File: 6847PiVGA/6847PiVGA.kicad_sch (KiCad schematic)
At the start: 51 parts, among them J1 DB15_Female_HighDensity, J2 Conn_01x06_Male, U1 MC6847, U2 AD724JRZ, U3 Pico, U4 AD813, U5 TXS0108EPW, U6 TXS0108EPW, U7 TXS0108EPW, Y1 4.433620MHz

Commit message: route out board
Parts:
- removed C11: 10uF, Capacitor_SMD:C_0805_2012Metric, symbol Device:C
- removed D1: 1N5817, Diode_SMD:D_0805_2012Metric_Pad1.15x1.40mm_HandSolder, symbol Diode:1N5817
- removed U3: Pico, Package_DIP:DIP-40_W15.24mm, symbol MCU_RaspberryPi_and_Boards:Pico
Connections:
- net +3.3V: no longer U5.10 (OE), U6.10 (OE), U7.10 (OE)
- net DD0: now also U5.14 (B6); no longer U5.20 (B1)
- net DD1: now also U5.15 (B5); no longer U5.18 (B2)
- net DD2: now also U5.16 (B4); no longer U5.17 (B3)
- net DD3: now also U5.17 (B3); no longer U5.16 (B4)
- net DD4: now also U5.18 (B2); no longer U5.15 (B5)
- net DD5: now also U5.20 (B1); no longer U5.14 (B6)
- net DL0: now also U5.7 (A6); no longer U5.1 (A1)
- net DL1: now also U5.6 (A5); no longer U5.3 (A2)
- net DL2: now also U5.5 (A4); no longer U5.4 (A3)
- net DL3: now also U5.4 (A3); no longer U5.5 (A4)
- net DL4: now also U5.3 (A2); no longer U5.6 (A5)
- net DL5: now also U5.1 (A1); no longer U5.7 (A6)
- net GND: no longer R23.2
- net G2: now reaches R6.2
- net G1: now reaches R5.2
- net B0: now reaches R7.2
- net R2: now reaches R3.2
- net B2: now reaches R9.2
- net B1: now reaches R8.2
- net G0: now reaches R4.2
- net R0: now reaches R1.2
- net R1: now reaches R2.2
- new net OE: R23.2, U5.10 (OE), U6.10 (OE), U7.10 (OE)
- no-connect marks 46 -> 42
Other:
- added sheet rp2040 (rp2040.kicad_sch)
- moved on the sheet: C12, C14, R23, U5

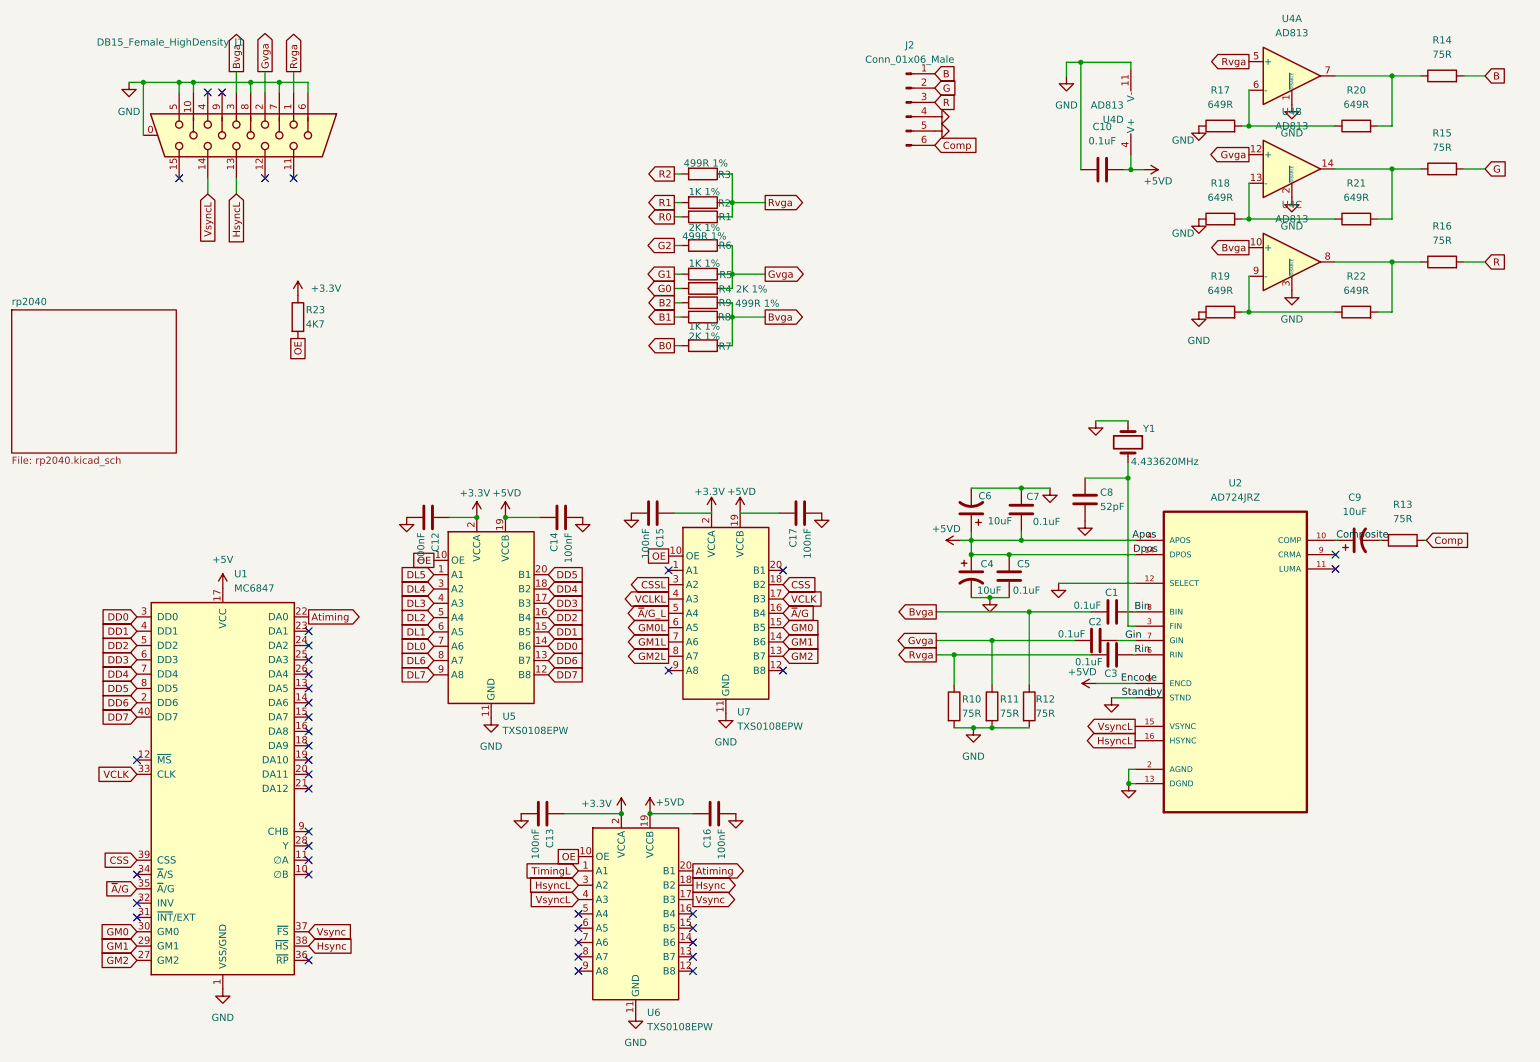
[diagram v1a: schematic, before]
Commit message: complete routing
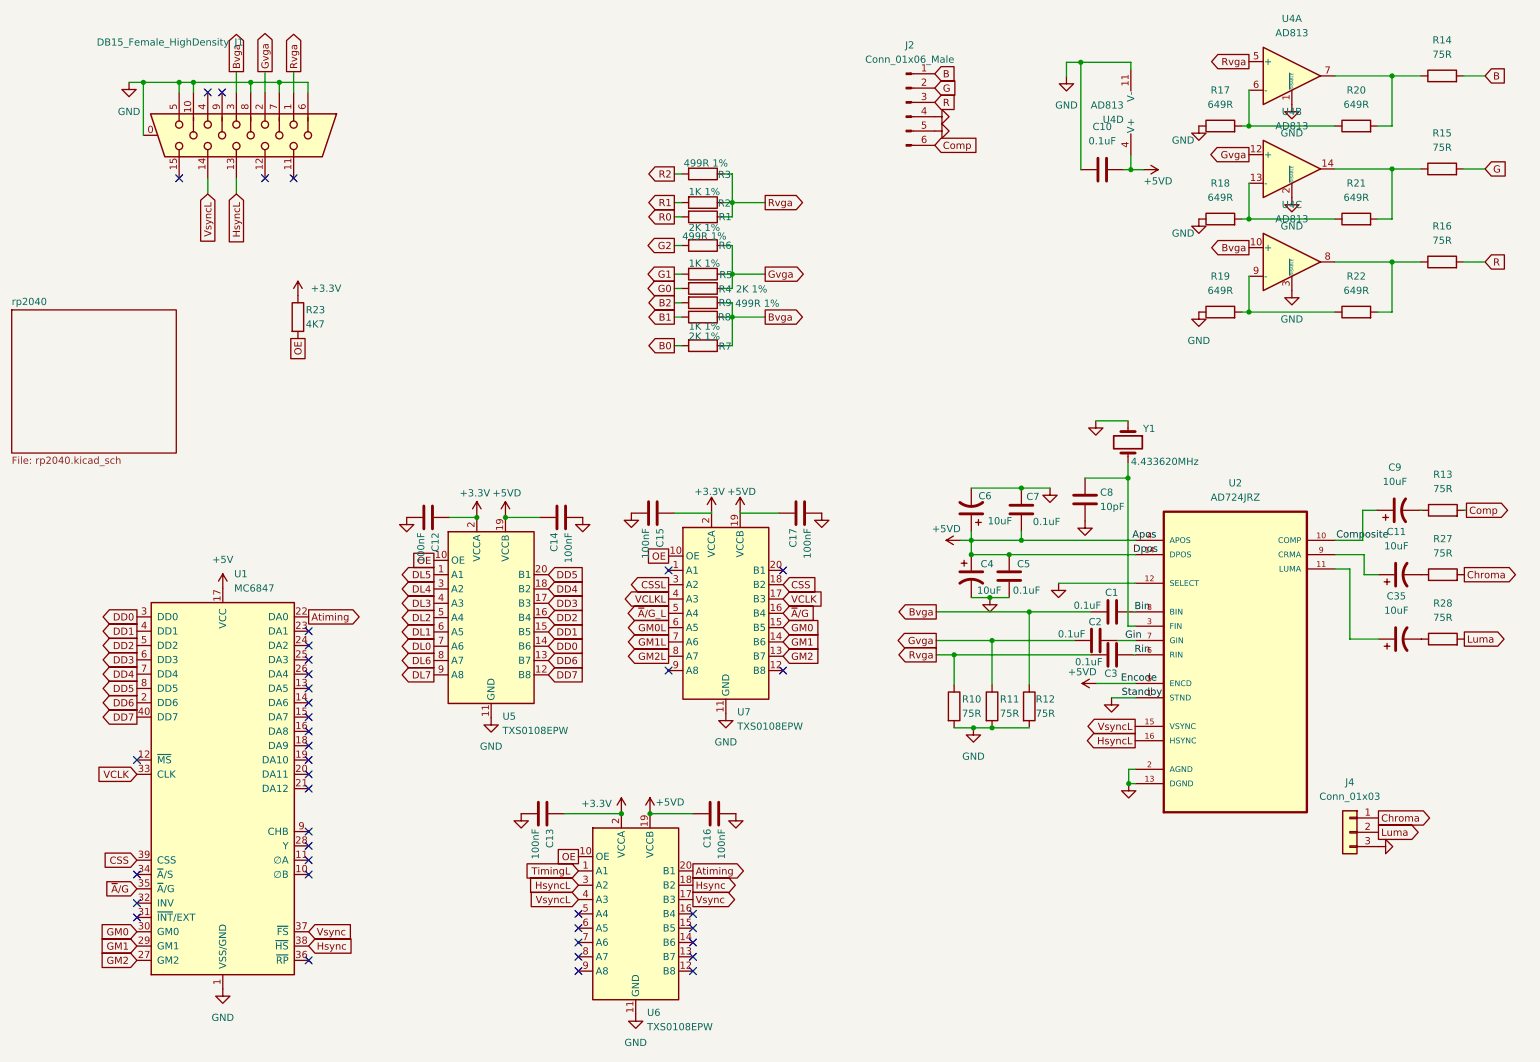
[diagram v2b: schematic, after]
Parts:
- added C11, C35: 10uF, Capacitor_Tantalum_SMD:CP_EIA-3216-10_Kemet-I_Pad1.58x1.35mm_HandSolder, symbol Device:C_Polarized_US
- added J4: Conn_01x03, Connector_PinHeader_2.54mm:PinHeader_1x03_P2.54mm_Vertical, symbol Connector_Generic:Conn_01x03
- added R27, R28: 75R, Resistor_SMD:R_0805_2012Metric, symbol Device:R
- C4, C6: footprint Capacitor_SMD:C_1206_3216Metric_Pad1.33x1.80mm_HandSolder -> Capacitor_Tantalum_SMD:CP_EIA-3216-10_Kemet-I_Pad1.58x1.35mm_HandSolder
- C8: value 52pF -> 10pF
- C9: footprint Capacitor_SMD:C_0805_2012Metric -> Capacitor_Tantalum_SMD:CP_EIA-3216-10_Kemet-I_Pad1.58x1.35mm_HandSolder
- U2: footprint AD724JRZ:SOIC127P1032X265-16N -> Package_SO:SOIC-16W_7.5x10.3mm_P1.27mm
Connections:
- net GND: now also J4.3 (Pin_3)
- net at U2.11 (LUMA): now also C35.1
- net at U2.9 (CRMA): now also C11.1
- new net: C11.2, R27.1
- new net: C35.2, R28.1
- new net Chroma: J4.1 (Pin_1), R27.2
- new net Luma: J4.2 (Pin_2), R28.2
- no-connect marks 42 -> 40
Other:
- moved on the sheet: C9, R13

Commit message: refine pcb routing
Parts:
- added R29: 100R, Resistor_SMD:R_0805_2012Metric, symbol Device:R
- R1, R4, R7: value 2K 1% -> 2K2 1%
- R3, R6, R9: value 499R 1% -> 470R 1%
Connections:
- net HsyncL: now also R29.2; no longer J1.13
- new net: J1.13, R29.1
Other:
- moved on the sheet: J1
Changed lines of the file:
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@@
 	)
 	(junction
-		(at 47.498 25.654)
+		(at 46.99 26.162)
 		(diameter 0)
 		(color 0 0 0 0)
 	)
 	(junction
-		(at 50.038 25.654)
+		(at 49.53 26.162)
 		(diameter 0)
 		(color 0 0 0 0)
@@
 	)
 	(junction
-		(at 41.148 25.654)
+		(at 40.64 26.162)
 		(diameter 0)
 		(color 0 0 0 0)
@@
 	)
 	(junction
-		(at 60.198 25.654)
+		(at 59.69 26.162)
 		(diameter 0)
 		(color 0 0 0 0)
@@
 	)
 	(junction
-		(at 65.278 25.654)
+		(at 64.77 26.162)
 		(diameter 0)
 		(color 0 0 0 0)
@@
 	)
 	(no_connect
-		(at 67.818 42.672)
+		(at 67.31 43.18)
 	)
 	(no_connect
-		(at 62.738 42.672)
+		(at 62.23 43.18)
 	)
 	(no_connect
-		(at 47.498 42.672)
+		(at 46.99 43.18)
 	)
 	(no_connect
-		(at 52.578 27.432)
+		(at 52.07 27.94)
 	)
 	(no_connect
-		(at 55.118 27.432)
+		(at 54.61 27.94)
 	)
 	(no_connect
@@
 	(wire
 		(pts
-			(xy 62.738 23.749) (xy 62.738 27.432)
+			(xy 62.23 24.257) (xy 62.23 27.94)
 		)
 		(stroke
@@
 	(wire
 		(pts
-			(xy 57.658 45.466) (xy 57.658 42.672)
-		)
-		(stroke
-			(width 0)
-			(type default)
-		)
-	)
-	(wire
-		(pts
 			(xy 186.182 106.934) (xy 188.087 106.934)
 		)
@@
 	(wire
 		(pts
-			(xy 67.818 23.749) (xy 67.818 27.432)
+			(xy 67.31 24.257) (xy 67.31 27.94)
 		)
 		(stroke
@@
 	(wire
 		(pts
-			(xy 50.038 25.654) (xy 47.498 25.654)
+			(xy 49.53 26.162) (xy 46.99 26.162)
 		)
 		(stroke
@@
 	(wire
 		(pts
-			(xy 50.038 25.654) (xy 50.038 27.432)
+			(xy 49.53 26.162) (xy 49.53 27.94)
 		)
 		(stroke
@@
 	(wire
 		(pts
-			(xy 41.148 25.654) (xy 47.498 25.654)
+			(xy 40.64 26.162) (xy 46.99 26.162)
 		)
 		(stroke
@@
 	(wire
 		(pts
-			(xy 60.198 27.432) (xy 60.198 25.654)
+			(xy 59.69 27.94) (xy 59.69 26.162)
 		)
 		(stroke
@@
 	(wire
 		(pts
-			(xy 57.658 23.749) (xy 57.658 27.432)
+			(xy 57.15 24.257) (xy 57.15 27.94)
 		)
 		(stroke
@@
 	(wire
 		(pts
-			(xy 38.608 25.654) (xy 41.148 25.654)
+			(xy 38.1 26.162) (xy 40.64 26.162)
 		)
 		(stroke
@@
 	(wire
 		(pts
-			(xy 41.148 25.654) (xy 41.148 35.052)
+			(xy 40.64 26.162) (xy 40.64 35.56)
 		)
 		(stroke
@@
 	(wire
 		(pts
-			(xy 60.198 25.654) (xy 65.278 25.654)
+			(xy 59.69 26.162) (xy 64.77 26.162)
 		)
 		(stroke
@@
 	(wire
 		(pts
-			(xy 47.498 25.654) (xy 47.498 27.432)
+			(xy 46.99 26.162) (xy 46.99 27.94)
 		)
 		(stroke
@@
 	(wire
 		(pts
-			(xy 65.278 25.654) (xy 65.278 27.432)
+			(xy 64.77 26.162) (xy 64.77 27.94)
 		)
 		(stroke
@@
 	(wire
 		(pts
-			(xy 70.358 25.654) (xy 65.278 25.654)
+			(xy 69.85 26.162) (xy 64.77 26.162)
 		)
 		(stroke
@@
 	(wire
 		(pts
-			(xy 52.578 45.466) (xy 52.578 42.672)
+			(xy 52.07 50.8) (xy 52.07 43.18)
 		)
 		(stroke
@@
 	(wire
 		(pts
-			(xy 70.358 27.432) (xy 70.358 25.654)
+			(xy 69.85 27.94) (xy 69.85 26.162)
 		)
 		(stroke
@@
 	(wire
 		(pts
-			(xy 60.198 25.654) (xy 50.038 25.654)
+			(xy 59.69 26.162) (xy 49.53 26.162)
 		)
 		(stroke
@@
 	(global_label "HsyncL"
 		(shape input)
-		(at 57.658 45.466 270)
+		(at 57.15 50.8 270)
 		(fields_autoplaced yes)
 		(effects
@@
 		)
 		(property "Intersheetrefs" "${INTERSHEET_REFS}"
-			(at 57.658 54.9637 90)
+			(at 57.15 60.2977 90)
 			(effects
 				(font
@@
 	(global_label "Gvga"
 		(shape output)
-		(at 62.738 23.749 90)
+		(at 62.23 24.257 90)
 		(fields_autoplaced yes)
 		(effects
@@
 		)
 		(property "Intersheetrefs" "${INTERSHEET_REFS}"
-			(at 62.6586 16.8002 90)
+			(at 62.1506 17.3082 90)
 			(effects
 				(font
@@
 	(global_label "Bvga"
 		(shape output)
-		(at 57.658 23.749 90)
+		(at 57.15 24.257 90)
 		(fields_autoplaced yes)
 		(effects
@@
 		)
 		(property "Intersheetrefs" "${INTERSHEET_REFS}"
-			(at 57.5786 16.8002 90)
+			(at 57.0706 17.3082 90)
 			(effects
 				(font
@@
 	(global_label "Rvga"
 		(shape output)
-		(at 67.818 23.749 90)
+		(at 67.31 24.257 90)
 		(fields_autoplaced yes)
 		(effects
@@
 		)
 		(property "Intersheetrefs" "${INTERSHEET_REFS}"
-			(at 67.7386 16.8002 90)
+			(at 67.2306 17.3082 90)
 			(effects
 				(font
@@
 	(global_label "VsyncL"
 		(shape input)
-		(at 52.578 45.466 270)
+		(at 52.07 50.8 270)
 		(fields_autoplaced yes)
 		(effects
@@
 		)
 		(property "Intersheetrefs" "${INTERSHEET_REFS}"
-			(at 52.578 54.7218 90)
+			(at 52.07 60.0558 90)
 			(effects
 				(font
@@
 			)
 		)
-		(property "Value" "499R 1%"
+		(property "Value" "470R 1%"
 			(at 140.716 52.959 90)
 			(effects
@@
 			)
 		)
-		(property "Value" "2K 1%"
+		(property "Value" "2K2 1%"
 			(at 140.716 70.739 90)
 			(effects
@@
 			)
 		)
-		(property "Value" "499R 1%"
+		(property "Value" "470R 1%"
 			(at 140.97 40.005 90)
 			(effects
@@
 	)
 	(symbol
+		(lib_id "Device:R")
+		(at 57.15 46.99 0)
+		(mirror y)
+		(unit 1)
+		(exclude_from_sim no)
+		(in_bom yes)
+		(on_board yes)
+		(dnp no)
+		(property "Reference" "R29"
+			(at 55.118 46.99 90)
+			(effects
+				(font
+					(size 1.27 1.27)
+				)
+			)
+		)
+		(property "Value" "100R"
+			(at 59.055 46.482 90)
+			(effects
+				(font
+					(size 1.27 1.27)
+				)
+			)
+		)
+		(property "Footprint" "Resistor_SMD:R_0805_2012Metric"
+			(at 58.928 46.99 90)
+			(effects
+				(font
+					(size 1.27 1.27)
+				)
+				(hide yes)
+			)
+		)
+		(property "Datasheet" "~"
+			(at 57.15 46.99 0)
+			(effects
+				(font
+					(size 1.27 1.27)
+				)
+				(hide yes)
+			)
+		)
+		(property "Description" ""
+			(at 57.15 46.99 0)
+			(effects
+				(font
+					(size 1.27 1.27)
+				)
+				(hide yes)
+			)
+		)
+		(pin "1"
+		)
+		(pin "2"
+		)
+		(instances
+			(project "6847PiVGA"
+				(path "/f0710b92-d288-438f-aac5-f4a9bf0cd905"
+					(reference "R29")
+					(unit 1)
+				)
+			)
+		)
+	)
+	(symbol
 		(lib_id "power:GND")
 		(at 108.204 155.448 0)
@@
 			)
 		)
-		(property "Value" "499R 1%"
+		(property "Value" "470R 1%"
 			(at 150.114 64.897 90)
 			(effects
@@
 	(symbol
 		(lib_id "power:GND")
-		(at 38.608 25.654 0)
+		(at 38.1 26.162 0)
 		(unit 1)
 		(exclude_from_sim no)
@@
 		(fields_autoplaced yes)
 		(property "Reference" "#PWR0109"
-			(at 38.608 32.004 0)
+			(at 38.1 32.512 0)
 			(effects
 				(font
@@
 		)
 		(property "Value" "GND"
-			(at 38.608 30.861 0)
+			(at 38.1 31.369 0)
 			(effects
 				(font
@@
 		)
 		(property "Footprint" ""
-			(at 38.608 25.654 0)
+			(at 38.1 26.162 0)
 			(effects
 				(font
@@
 		)
 		(property "Datasheet" ""
-			(at 38.608 25.654 0)
+			(at 38.1 26.162 0)
 			(effects
 				(font
@@
 		)
 		(property "Description" ""
-			(at 38.608 25.654 0)
+			(at 38.1 26.162 0)
 			(effects
 				(font
@@
 			)
 		)
-		(property "Value" "2K 1%"
+		(property "Value" "2K2 1%"
 			(at 149.098 62.357 90)
 			(effects
@@
 			)
 		)
-		(property "Value" "2K 1%"
+		(property "Value" "2K2 1%"
 			(at 140.716 51.435 90)
 			(effects
@@
 	(symbol
 		(lib_id "Connector:DB15_Female_HighDensity")
-		(at 57.658 35.052 270)
+		(at 57.15 35.56 270)
 		(unit 1)
 		(exclude_from_sim no)
@@
 		(fields_autoplaced yes)
 		(property "Reference" "J1"
-			(at 58.9281 18.542 90)
+			(at 58.4201 19.05 90)
 			(effects
 				(font
@@
 		)
 		(property "Value" "DB15_Female_HighDensity"
-			(at 56.3881 18.542 90)
+			(at 55.8801 19.05 90)
 			(effects
 				(font
@@
 		)
 		(property "Footprint" "Connector_Dsub:DSUB-15-HD_Female_Horizontal_P2.29x1.98mm_EdgePinOffset3.03mm_Housed_MountingHolesOffset4.94mm"
-			(at 81.788 45.212 0)
+			(at 81.28 45.72 0)
 			(effects
 				(font
@@
 		)
 		(property "Datasheet" " ~"
-			(at 81.788 45.212 0)
+			(at 81.28 45.72 0)
 			(effects
 				(font
@@
 		)
 		(property "Description" ""
-			(at 57.658 35.052 0)
+			(at 57.15 35.56 0)
 			(effects
 				(font

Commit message: update readme
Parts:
- added TP4: Audio, TestPoint:TestPoint_Loop_D1.80mm_Drill1.0mm_Beaded, symbol Connector:TestPoint
- J4: footprint Connector_PinHeader_2.54mm:PinHeader_1x03_P2.54mm_Vertical -> Connector_PinHeader_2.54mm:PinHeader_1x04_P2.54mm_Vertical; symbol Connector_Generic:Conn_01x03 -> Connector_Generic:Conn_01x04
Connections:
- new net AUDIO: J4.4 (Pin_4), TP4.1
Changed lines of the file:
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@@
 		)
 	)
+	(global_label "AUDIO"
+		(shape input)
+		(at 198.12 161.29 0)
+		(fields_autoplaced yes)
+		(effects
+			(font
+				(size 1.27 1.27)
+			)
+			(justify left)
+		)
+		(property "Intersheetrefs" "${INTERSHEET_REFS}"
+			(at 206.7296 161.29 0)
+			(effects
+				(font
+					(size 1.27 1.27)
+				)
+				(justify left)
+				(hide yes)
+			)
+		)
+	)
 	(global_label "DD0"
 		(shape output)
@@
 		)
 	)
+	(global_label "AUDIO"
+		(shape output)
+		(at 260.35 163.83 0)
+		(fields_autoplaced yes)
+		(effects
+			(font
+				(size 1.27 1.27)
+			)
+			(justify left)
+		)
+		(property "Intersheetrefs" "${INTERSHEET_REFS}"
+			(at 268.9596 163.83 0)
+			(effects
+				(font
+					(size 1.27 1.27)
+				)
+				(justify left)
+				(hide yes)
+			)
+		)
+	)
 	(global_label "Hsync"
 		(shape input)
@@
 	)
 	(symbol
+		(lib_id "Connector:TestPoint")
+		(at 198.12 161.29 90)
+		(unit 1)
+		(exclude_from_sim no)
+		(in_bom yes)
+		(on_board yes)
+		(dnp no)
+		(fields_autoplaced yes)
+		(property "Reference" "TP4"
+			(at 194.818 156.21 90)
+			(effects
+				(font
+					(size 1.27 1.27)
+				)
+			)
+		)
+		(property "Value" "Audio"
+			(at 194.818 158.75 90)
+			(effects
+				(font
+					(size 1.27 1.27)
+				)
+			)
+		)
+		(property "Footprint" "TestPoint:TestPoint_Loop_D1.80mm_Drill1.0mm_Beaded"
+			(at 198.12 156.21 0)
+			(effects
+				(font
+					(size 1.27 1.27)
+				)
+				(hide yes)
+			)
+		)
+		(property "Datasheet" "~"
+			(at 198.12 156.21 0)
+			(effects
+				(font
+					(size 1.27 1.27)
+				)
+				(hide yes)
+			)
+		)
+		(property "Description" "test point"
+			(at 198.12 161.29 0)
+			(effects
+				(font
+					(size 1.27 1.27)
+				)
+				(hide yes)
+			)
+		)
+		(pin "1"
+		)
+		(instances
+			(project "6847PiVGA"
+				(path "/f0710b92-d288-438f-aac5-f4a9bf0cd905"
+					(reference "TP4")
+					(unit 1)
+				)
+			)
+		)
+	)
+	(symbol
 		(lib_id "Device:R")
 		(at 140.462 72.39 270)
@@
 	)
 	(symbol
-		(lib_id "Connector_Generic:Conn_01x03")
+		(lib_id "Connector_Generic:Conn_01x04")
 		(at 255.27 158.75 0)
 		(mirror y)
@@
 			)
 		)
-		(property "Footprint" "Connector_PinHeader_2.54mm:PinHeader_1x03_P2.54mm_Vertical"
+		(property "Footprint" "Connector_PinHeader_2.54mm:PinHeader_1x04_P2.54mm_Vertical"
 			(at 255.27 158.75 0)
 			(effects
@@
 			)
 		)
-		(property "Description" "Generic connector, single row, 01x03, script generated (kicad-library-utils/schlib/autogen/connector/)"
+		(property "Description" "Generic connector, single row, 01x04, script generated (kicad-library-utils/schlib/autogen/connector/)"
 			(at 255.27 158.75 0)
 			(effects
@@
 		(pin "1"
 		)
+		(pin "4"
+		)
 		(instances
